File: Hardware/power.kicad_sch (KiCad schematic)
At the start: 17 parts, among them J1 I2C Debug, J2 I2C, J3 I2C, U3 LM285D-2.5, U7 AP7312-1833W6-7

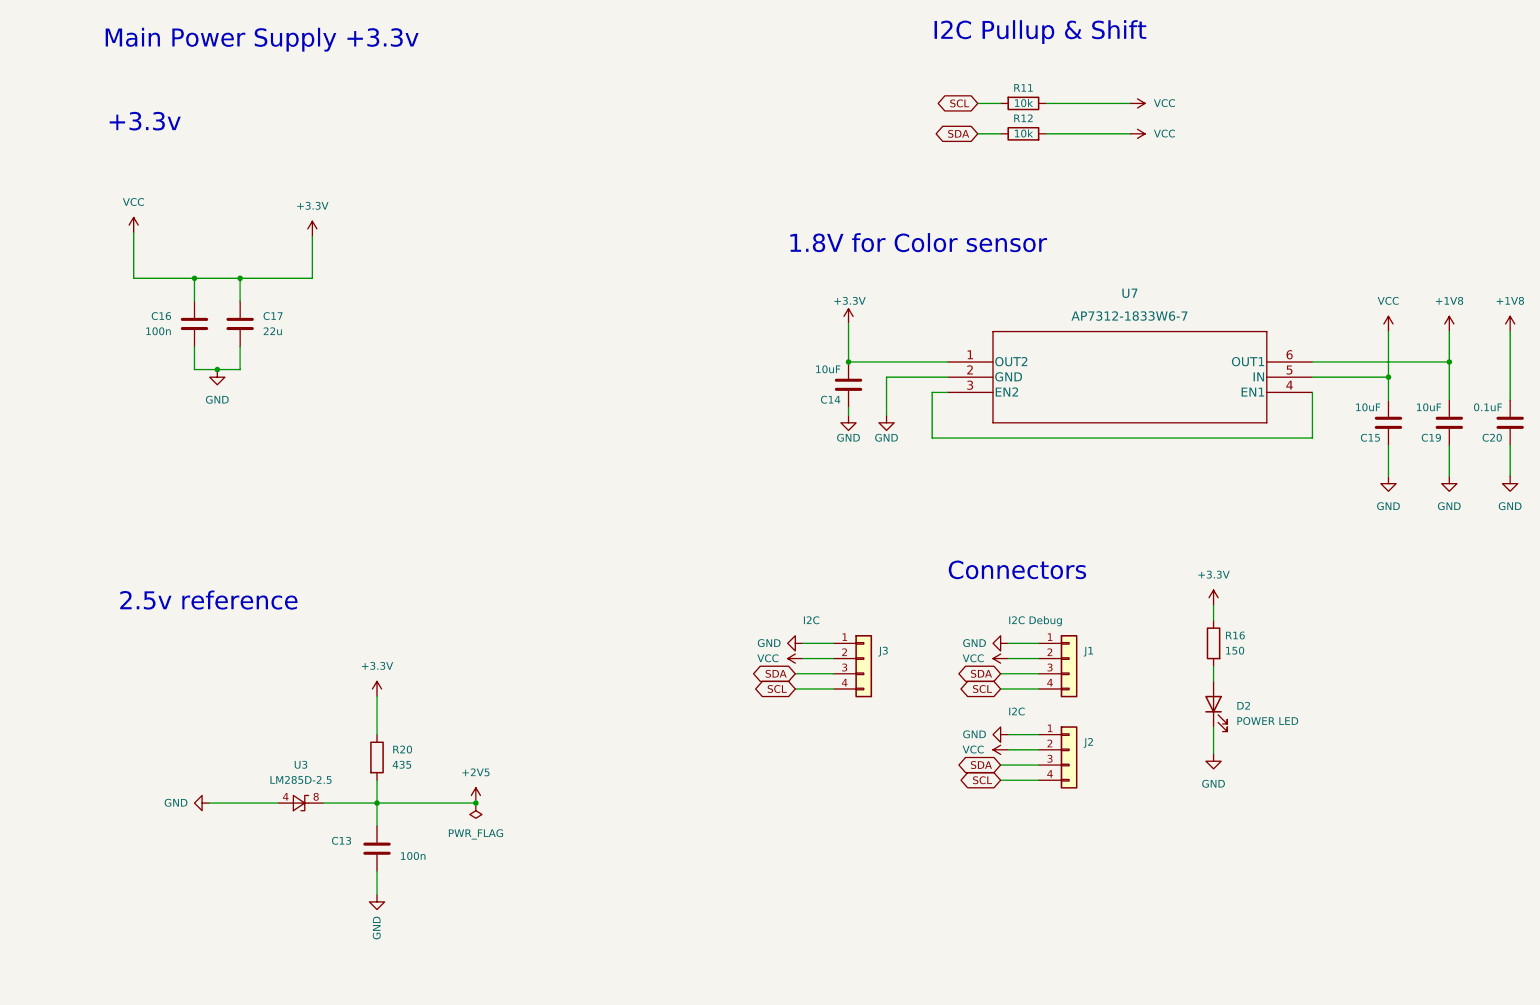
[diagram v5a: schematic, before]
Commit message: removed 2.5v circuit to use the built in variable ldo on the ADC added ~4.915Mhz crystal for 50/60Hz filtering fixed several small schematic issues completely relaid out the board.
Signed-off-by: lokimetasmith <lokimail@gmail.com>
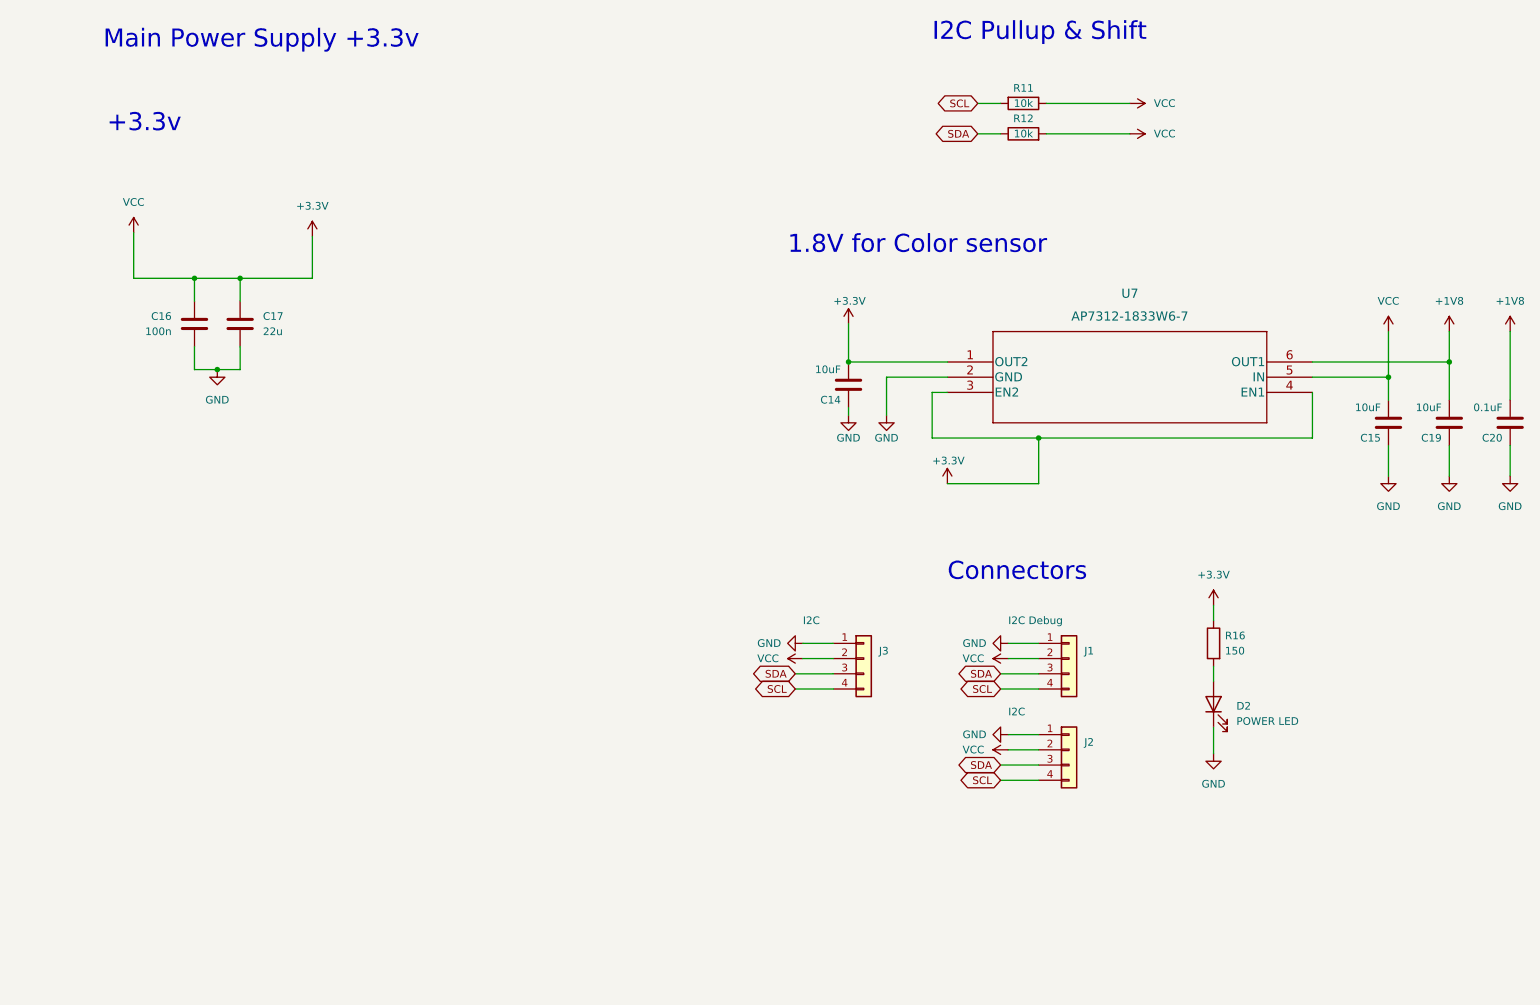
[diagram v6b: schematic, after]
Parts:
- removed C13: 100n, Capacitor_SMD:C_0603_1608Metric_Pad1.08x0.95mm_HandSolder, symbol Device:C
- removed R20: 435, Resistor_SMD:R_0603_1608Metric_Pad0.98x0.95mm_HandSolder, symbol Device:R
- removed U3: LM285D-2.5, Package_SO:SOIC-8_3.9x4.9mm_P1.27mm, symbol Reference_Voltage:LM285D-2.5
- J1: footprint Connector_PinHeader_2.54mm:PinHeader_1x04_P2.54mm_Vertical -> Connector_PinSocket_1.27mm:PinSocket_1x04_P1.27mm_Vertical
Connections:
- net +3V3: now also U7.3 (EN2), U7.4 (EN1)
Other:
- note removed: "2.5v reference"
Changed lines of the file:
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@@
   (junction (at 250.19 92.71) (diameter 0) (color 0 0 0 0)
   )
-  (junction (at 81.28 163.83) (diameter 0) (color 0 0 0 0)
-  )
   (junction (at 58.42 76.2) (diameter 0) (color 0 0 0 0)
   )
-  (junction (at 97.79 163.83) (diameter 0) (color 0 0 0 0)
+  (junction (at 191.77 102.87) (diameter 0) (color 0 0 0 0)
   )
   (junction (at 54.61 91.44) (diameter 0) (color 0 0 0 0)
@@
     (stroke (width 0) (type default) (color 0 0 0 0))
   )
-  (wire (pts (xy 237.49 102.87) (xy 173.99 102.87))
-    (stroke (width 0) (type default) (color 0 0 0 0))
-  )
-  (wire (pts (xy 72.39 163.83) (xy 81.28 163.83))
+  (wire (pts (xy 237.49 102.87) (xy 191.77 102.87))
     (stroke (width 0) (type default) (color 0 0 0 0))
   )
@@
     (stroke (width 0) (type default) (color 0 0 0 0))
   )
-  (wire (pts (xy 81.28 175.26) (xy 81.28 179.07))
-    (stroke (width 0) (type default) (color 0 0 0 0))
-  )
   (wire (pts (xy 270.51 104.14) (xy 270.51 109.22))
     (stroke (width 0) (type default) (color 0 0 0 0))
@@
     (stroke (width 0) (type default) (color 0 0 0 0))
   )
-  (wire (pts (xy 53.34 163.83) (xy 64.77 163.83))
-    (stroke (width 0) (type default) (color 0 0 0 0))
-  )
   (wire (pts (xy 166.37 92.71) (xy 166.37 99.06))
     (stroke (width 0) (type default) (color 0 0 0 0))
@@
     (stroke (width 0) (type default) (color 0 0 0 0))
   )
-  (wire (pts (xy 81.28 160.02) (xy 81.28 163.83))
-    (stroke (width 0) (type default) (color 0 0 0 0))
-  )
   (wire (pts (xy 260.35 90.17) (xy 260.35 96.52))
     (stroke (width 0) (type default) (color 0 0 0 0))
@@
     (stroke (width 0) (type default) (color 0 0 0 0))
   )
-  (wire (pts (xy 81.28 163.83) (xy 81.28 167.64))
-    (stroke (width 0) (type default) (color 0 0 0 0))
-  )
   (wire (pts (xy 70.485 69.215) (xy 70.485 76.2))
     (stroke (width 0) (type default) (color 0 0 0 0))
   )
-  (wire (pts (xy 81.28 146.05) (xy 81.28 152.4))
-    (stroke (width 0) (type default) (color 0 0 0 0))
-  )
   (wire (pts (xy 50.8 76.2) (xy 58.42 76.2))
     (stroke (width 0) (type default) (color 0 0 0 0))
   )
-  (wire (pts (xy 81.28 163.83) (xy 97.79 163.83))
+  (wire (pts (xy 191.77 110.49) (xy 191.77 102.87))
     (stroke (width 0) (type default) (color 0 0 0 0))
   )
@@
     (stroke (width 0) (type default) (color 0 0 0 0))
   )
+  (wire (pts (xy 176.53 110.49) (xy 191.77 110.49))
+    (stroke (width 0) (type default) (color 0 0 0 0))
+  )
   (wire (pts (xy 160.02 90.17) (xy 176.53 90.17))
     (stroke (width 0) (type default) (color 0 0 0 0))
@@
   )
   (wire (pts (xy 186.69 139.7) (xy 191.77 139.7))
+    (stroke (width 0) (type default) (color 0 0 0 0))
+  )
+  (wire (pts (xy 191.77 102.87) (xy 173.99 102.87))
     (stroke (width 0) (type default) (color 0 0 0 0))
   )
@@
   )
   (text "Main Power Supply +3.3v" (at 35.56 38.1 0)
-    (effects (font (size 3 3)) (justify left bottom))
-  )
-  (text "2.5v reference" (at 38.1 132.08 0)
     (effects (font (size 3 3)) (justify left bottom))
   )
@@
     (pin "2")
   )
-  (symbol (lib_id "Reference_Voltage:LM285D-2.5") (at 68.58 163.83 0) (unit 1)
-    (in_bom yes) (on_board yes) (fields_autoplaced)
-    (property "Reference" "U3" (id 0) (at 68.58 157.48 0))
-    (property "Value" "LM285D-2.5" (id 1) (at 68.58 160.02 0))
-    (property "Footprint" "Package_SO:SOIC-8_3.9x4.9mm_P1.27mm" (id 2) (at 68.58 168.91 0)
-      (effects (font (size 1.27 1.27) italic) hide)
-    )
-    (property "Datasheet" "http://www.onsemi.com/pub_link/Collateral/LM285-D.PDF" (id 3) (at 68.58 163.83 0)
-      (effects (font (size 1.27 1.27) italic) hide)
-    )
-    (pin "4")
-    (pin "8")
-  )
   (symbol (lib_id "power:GND") (at 186.69 137.16 270) (unit 1)
     (in_bom yes) (on_board yes)
@@
     (pin "1")
   )
+  (symbol (lib_id "power:+3.3V") (at 176.53 110.49 0) (unit 1)
+    (in_bom yes) (on_board yes)
+    (property "Reference" "#PWR0132" (id 0) (at 176.53 114.3 0)
+      (effects (font (size 1.27 1.27)) hide)
+    )
+    (property "Value" "+3.3V" (id 1) (at 173.99 106.68 0)
+      (effects (font (size 1.27 1.27)) (justify left))
+    )
+    (property "Footprint" "" (id 2) (at 176.53 110.49 0)
+      (effects (font (size 1.27 1.27)) hide)
+    )
+    (property "Datasheet" "" (id 3) (at 176.53 110.49 0)
+      (effects (font (size 1.27 1.27)) hide)
+    )
+    (pin "1")
+  )
   (symbol (lib_id "power:VCC") (at 186.69 139.7 90) (unit 1)
     (in_bom yes) (on_board yes)
@@
     (pin "1")
   )
-  (symbol (lib_id "Device:C") (at 81.28 171.45 0) (unit 1)
-    (in_bom yes) (on_board yes)
-    (property "Reference" "C13" (id 0) (at 73.66 170.1799 0)
-      (effects (font (size 1.27 1.27)) (justify left))
-    )
-    (property "Value" "100n" (id 1) (at 85.09 172.7199 0)
-      (effects (font (size 1.27 1.27)) (justify left))
-    )
-    (property "Footprint" "Capacitor_SMD:C_0603_1608Metric_Pad1.08x0.95mm_HandSolder" (id 2) (at 82.2452 175.26 0)
-      (effects (font (size 1.27 1.27)) hide)
-    )
-    (property "Datasheet" "~" (id 3) (at 81.28 171.45 0)
-      (effects (font (size 1.27 1.27)) hide)
-    )
-    (pin "1")
-    (pin "2")
-  )
   (symbol (lib_id "Connector_Generic:Conn_01x04") (at 162.56 139.7 0) (unit 1)
     (in_bom yes) (on_board yes)
@@
     )
     (property "Datasheet" "" (id 3) (at 270.51 85.09 0)
-      (effects (font (size 1.27 1.27)) hide)
-    )
-    (pin "1")
-  )
-  (symbol (lib_id "power:PWR_FLAG") (at 97.79 163.83 0) (mirror x) (unit 1)
-    (in_bom yes) (on_board yes) (fields_autoplaced)
-    (property "Reference" "#FLG02" (id 0) (at 97.79 165.735 0)
-      (effects (font (size 1.27 1.27)) hide)
-    )
-    (property "Value" "PWR_FLAG" (id 1) (at 97.79 168.91 0))
-    (property "Footprint" "" (id 2) (at 97.79 163.83 0)
-      (effects (font (size 1.27 1.27)) hide)
-    )
-    (property "Datasheet" "~" (id 3) (at 97.79 163.83 0)
       (effects (font (size 1.27 1.27)) hide)
     )
@@
     (pin "2")
   )
-  (symbol (lib_id "Device:R") (at 81.28 156.21 0) (unit 1)
-    (in_bom yes) (on_board yes) (fields_autoplaced)
-    (property "Reference" "R20" (id 0) (at 83.82 154.9399 0)
-      (effects (font (size 1.27 1.27)) (justify left))
-    )
-    (property "Value" "435" (id 1) (at 83.82 157.4799 0)
-      (effects (font (size 1.27 1.27)) (justify left))
-    )
-    (property "Footprint" "Resistor_SMD:R_0603_1608Metric_Pad0.98x0.95mm_HandSolder" (id 2) (at 79.502 156.21 90)
-      (effects (font (size 1.27 1.27)) hide)
-    )
-    (property "Datasheet" "~" (id 3) (at 81.28 156.21 0)
-      (effects (font (size 1.27 1.27)) hide)
-    )
-    (pin "1")
-    (pin "2")
-  )
-  (symbol (lib_id "power:GND") (at 53.34 163.83 270) (unit 1)
-    (in_bom yes) (on_board yes)
-    (property "Reference" "#PWR0118" (id 0) (at 46.99 163.83 0)
-      (effects (font (size 1.27 1.27)) hide)
-    )
-    (property "Value" "GND" (id 1) (at 45.72 163.83 90)
-      (effects (font (size 1.27 1.27)) (justify left))
-    )
-    (property "Footprint" "" (id 2) (at 53.34 163.83 0)
-      (effects (font (size 1.27 1.27)) hide)
-    )
-    (property "Datasheet" "" (id 3) (at 53.34 163.83 0)
-      (effects (font (size 1.27 1.27)) hide)
-    )
-    (pin "1")
-  )
   (symbol (lib_id "power:+3.3V") (at 220.98 130.81 0) (unit 1)
     (in_bom yes) (on_board yes)
@@
     (pin "1")
   )
-  (symbol (lib_id "power:+3.3V") (at 81.28 146.05 0) (unit 1)
-    (in_bom yes) (on_board yes) (fields_autoplaced)
-    (property "Reference" "#PWR0132" (id 0) (at 81.28 149.86 0)
-      (effects (font (size 1.27 1.27)) hide)
-    )
-    (property "Value" "+3.3V" (id 1) (at 81.28 140.97 0))
-    (property "Footprint" "" (id 2) (at 81.28 146.05 0)
-      (effects (font (size 1.27 1.27)) hide)
-    )
-    (property "Datasheet" "" (id 3) (at 81.28 146.05 0)
-      (effects (font (size 1.27 1.27)) hide)
-    )
-    (pin "1")
-  )
   (symbol (lib_id "Device:LED") (at 220.98 147.32 90) (unit 1)
     (in_bom yes) (on_board yes) (fields_autoplaced)
@@
     (pin "1")
     (pin "2")
-  )
-  (symbol (lib_id "power:+2V5") (at 97.79 163.83 0) (unit 1)
-    (in_bom yes) (on_board yes) (fields_autoplaced)
-    (property "Reference" "#PWR029" (id 0) (at 97.79 167.64 0)
-      (effects (font (size 1.27 1.27)) hide)
-    )
-    (property "Value" "+2V5" (id 1) (at 97.79 158.75 0))
-    (property "Footprint" "" (id 2) (at 97.79 163.83 0)
-      (effects (font (size 1.27 1.27)) hide)
-    )
-    (property "Datasheet" "" (id 3) (at 97.79 163.83 0)
-      (effects (font (size 1.27 1.27)) hide)
-    )
-    (pin "1")
   )
   (symbol (lib_id "power:+3.3V") (at 70.485 69.215 0) (unit 1)
@@
       (effects (font (size 1.27 1.27)) (justify left))
     )
-    (property "Footprint" "Connector_PinHeader_2.54mm:PinHeader_1x04_P2.54mm_Vertical" (id 2) (at 196.85 139.7 0)
+    (property "Footprint" "Connector_PinSocket_1.27mm:PinSocket_1x04_P1.27mm_Vertical" (id 2) (at 196.85 139.7 0)
       (effects (font (size 1.27 1.27)) hide)
     )
@@
     (pin "4")
   )
-  (symbol (lib_id "power:GND") (at 81.28 179.07 0) (unit 1)
-    (in_bom yes) (on_board yes)
-    (property "Reference" "#PWR014" (id 0) (at 81.28 185.42 0)
-      (effects (font (size 1.27 1.27)) hide)
-    )
-    (property "Value" "GND" (id 1) (at 81.28 186.69 90)
-      (effects (font (size 1.27 1.27)) (justify left))
-    )
-    (property "Footprint" "" (id 2) (at 81.28 179.07 0)
-      (effects (font (size 1.27 1.27)) hide)
-    )
-    (property "Datasheet" "" (id 3) (at 81.28 179.07 0)
-      (effects (font (size 1.27 1.27)) hide)
-    )
-    (pin "1")
-  )
   (symbol (lib_id "power:GND") (at 152.4 137.16 270) (unit 1)

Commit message: added -backups to gitignore lots of layout changes.
Signed-off-by: lokimetasmith <lokimail@gmail.com>
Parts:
- J1: footprint Connector_PinSocket_1.27mm:PinSocket_1x04_P1.27mm_Vertical -> Connector_PinSocket_2.54mm:PinSocket_1x04_P2.54mm_Vertical
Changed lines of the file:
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@@
       (effects (font (size 1.27 1.27)) (justify left))
     )
-    (property "Footprint" "Connector_PinSocket_1.27mm:PinSocket_1x04_P1.27mm_Vertical" (id 2) (at 196.85 139.7 0)
+    (property "Footprint" "Connector_PinSocket_2.54mm:PinSocket_1x04_P2.54mm_Vertical" (id 2) (at 196.85 139.7 0)
       (effects (font (size 1.27 1.27)) hide)
     )
